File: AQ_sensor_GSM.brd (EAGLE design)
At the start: 110 x 64 mm, 49 parts, among them IC2 MCP73831/OT, J1 F-1X03-SIP-100-32, SW1 PCM12SMTR, SW2 PCM12SMTR, U2 TEXAS_INSTRUMENTS_SN74HC125TE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, U3 TEXAS_INSTRUMENTS_LM1117IMP-3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, X1 53048-08, X2 SIMLOCK-C707_10M006_512_2, X4 50 Ohms

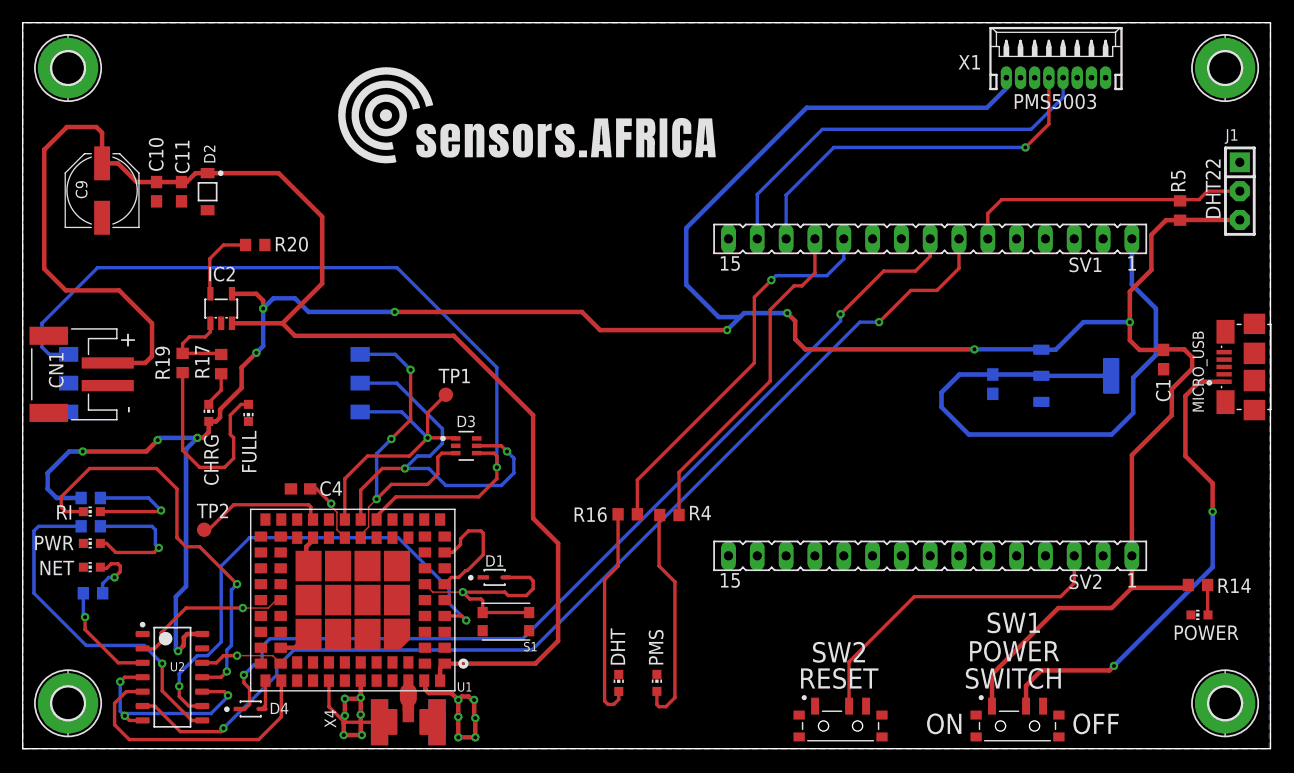
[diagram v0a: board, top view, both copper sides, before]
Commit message: Optimized power planes
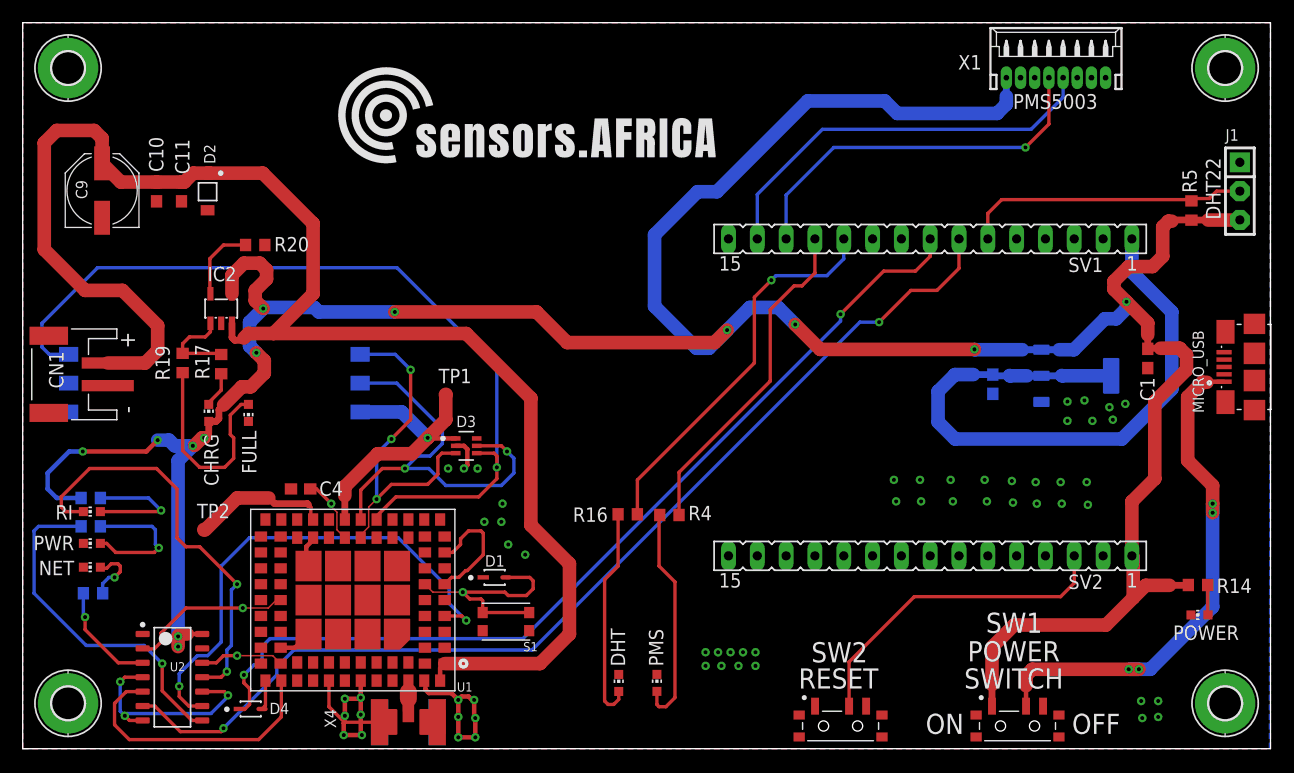
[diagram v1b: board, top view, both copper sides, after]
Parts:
- moved C1 1.40 mm to (99.2, 34.4)
- moved R5 1.00 mm to (103.0, 47.4)
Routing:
- net +5V: track 257.8 -> 276.6 mm, vias 11 -> 13
- net +3V3: track 52.7 -> 56.9 mm
- net VIN: track 42.6 -> 46.5 mm, vias 2 -> 4
- net GND: track 68.6 -> 71.6 mm, vias 15 -> 59
- net V_LIPO: track 133.9 -> 136.5 mm
- net 2.8V: track 11.6 -> 12.7 mm
